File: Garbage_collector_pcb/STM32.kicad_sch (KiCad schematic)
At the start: 26 parts, among them J2 Conn_ST_STDC14, SW2 SW_Push, U2 BQ25896RTWR, Y2 24MHz, Y3 32KHz

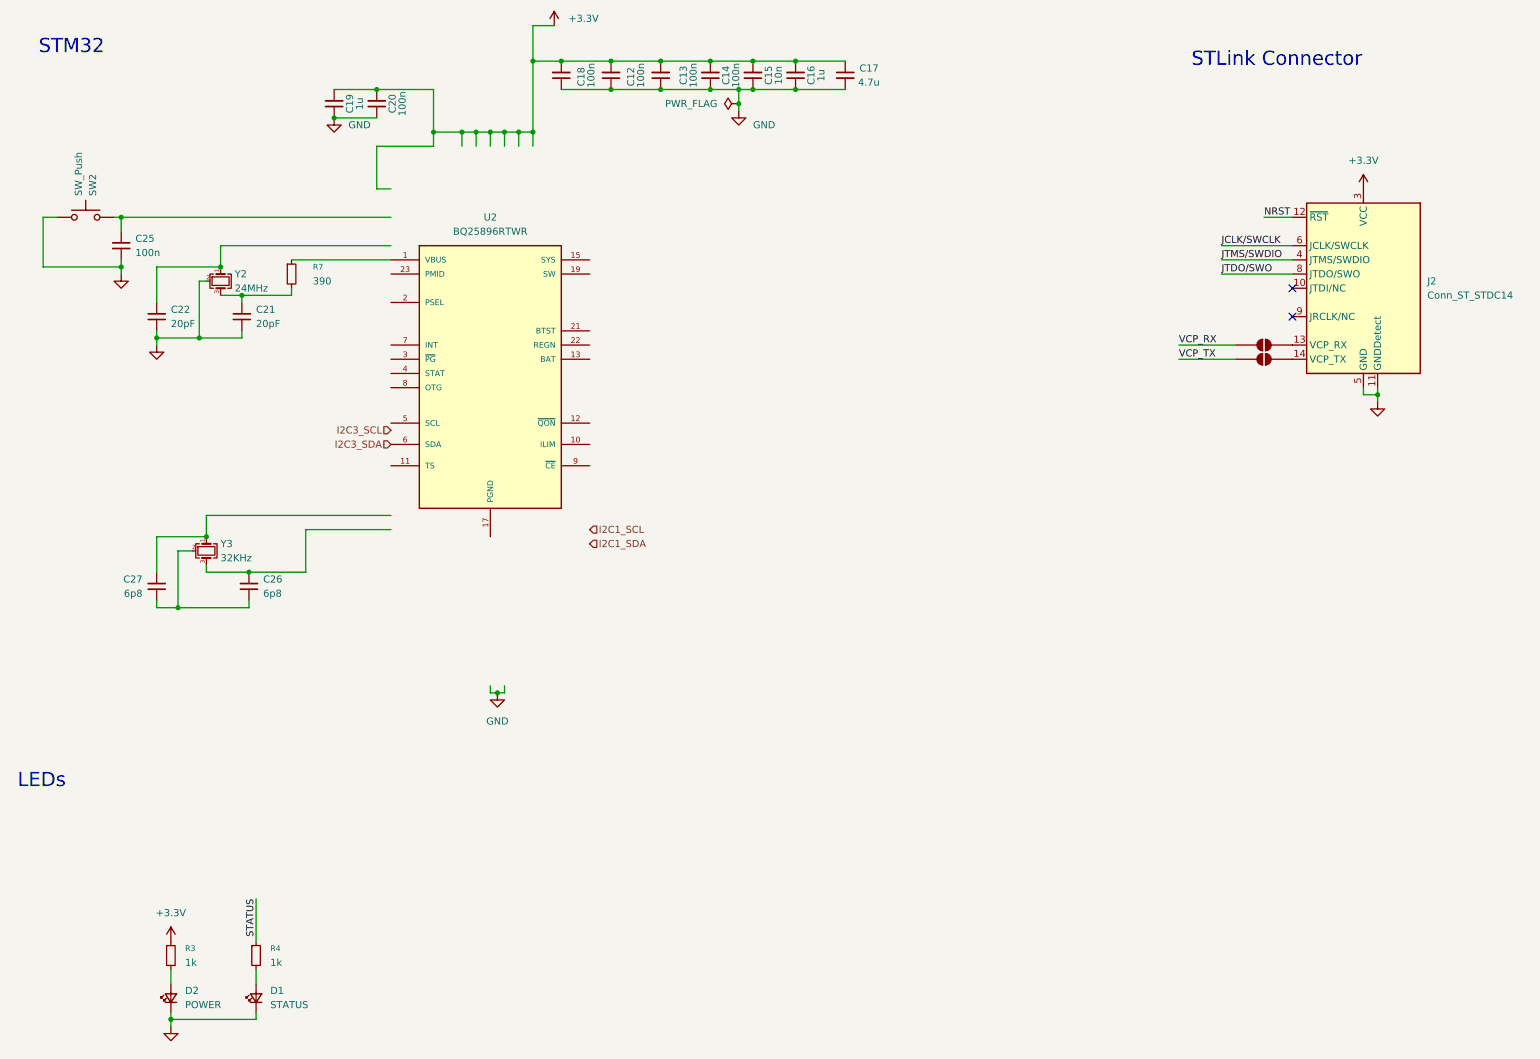
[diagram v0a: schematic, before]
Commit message: update MCU+Moteurs+Capteurs parts + assignement des labels + assignement des pins sur l'ioc (CubeMX)
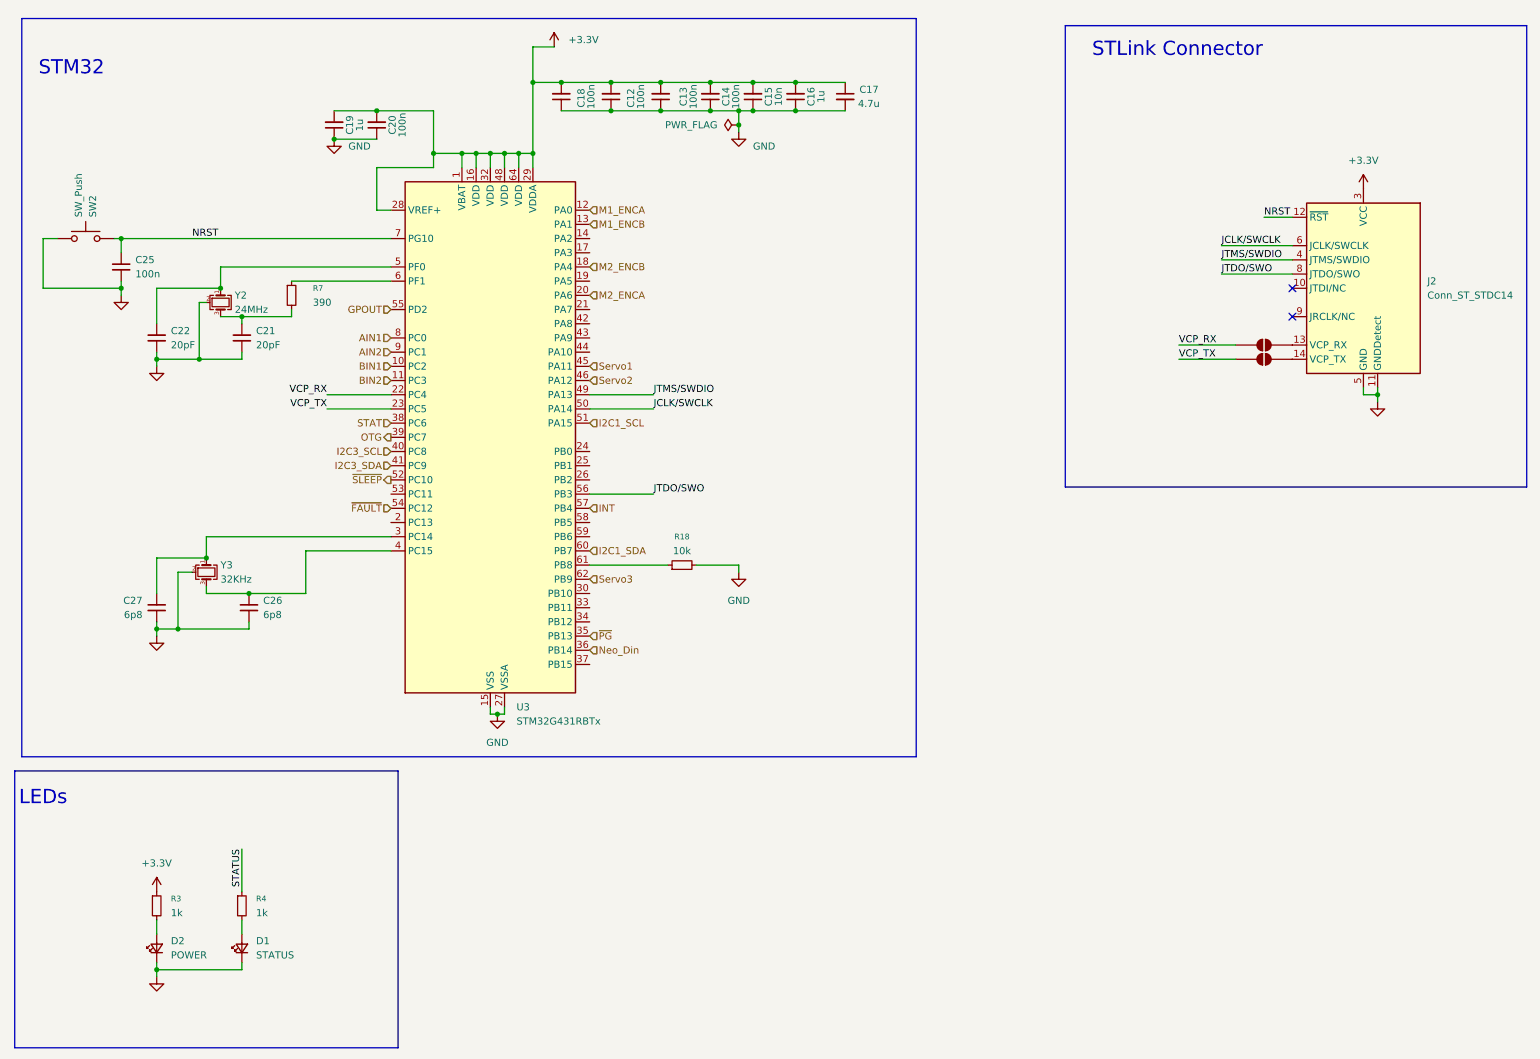
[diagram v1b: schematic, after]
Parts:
- removed U2: BQ25896RTWR, Package_DFN_QFN:Texas_RTW_WQFN-24-1EP_4x4mm_P0.5mm_EP2.7x2.7mm, symbol MCU_ST_STM32G4:STM32G431RBTx
- added R18: 10k, Resistor_THT:R_Array_SIP4, symbol Device:R_Small
- added U3: STM32G431RBTx, Package_QFP:LQFP-64_10x10mm_P0.5mm, symbol MCU_ST_STM32G4:STM32G431RBTx
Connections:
- net +3.3V: now also U3.1 (VBAT), U3.16 (VDD), U3.28 (VREF+), U3.29 (VDDA), U3.32 (VDD), U3.48 (VDD), U3.64 (VDD)
- net GND: now also C26.2, C27.2, Y3.2 (G), Y3.4 (G), R18.2, U3.15 (VSS), U3.27 (VSSA), U3.31 (VSS), U3.47 (VSS), U3.63 (VSS)
- net I2C1_SCL: now also U3.51 (PA15)
- net I2C1_SDA: now also U3.60 (PB7)
- net I2C3_SCL: now also U3.40 (PC8)
- net I2C3_SDA: now also U3.41 (PC9)
- net JCLK/SWCLK: now also U3.50 (PA14)
- net JTDO/SWO: now also U3.56 (PB3)
- net JTMS/SWDIO: now also U3.49 (PA13)
- net NRST: now also C25.1, SW2.1, U3.7 (PG10)
- net VCP_RX: now also U3.22 (PC4)
- net VCP_TX: now also U3.23 (PC5)
- net at C27.1, Y3.1: now also U3.3 (PC14)
- net at C22.1, Y2.1: now also U3.5 (PF0)
- net at R7.1: now also U3.6 (PF1)
- net at C26.1, Y3.3: now also U3.4 (PC15)
- new net: R18.1, U3.61 (PB8)
- new net AIN1: U3.8 (PC0)
- new net AIN2: U3.9 (PC1)
- new net BIN1: U3.10 (PC2)
- new net BIN2: U3.11 (PC3)
- new net GPOUT: U3.55 (PD2)
- new net INT: U3.57 (PB4)
- new net M1_ENCA: U3.12 (PA0)
- new net M1_ENCB: U3.13 (PA1)
- new net M2_ENCA: U3.20 (PA6)
- new net M2_ENCB: U3.18 (PA4)
- new net Neo_Din: U3.36 (PB14)
- new net OTG: U3.39 (PC7)
- new net STAT: U3.38 (PC6)
- new net Servo1: U3.45 (PA11)
- new net Servo2: U3.46 (PA12)
- new net Servo3: U3.62 (PB9)
- new net ~{FAULT}: U3.54 (PC12)
- new net ~{PG}: U3.35 (PB13)
- new net ~{SLEEP}: U3.52 (PC10)
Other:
- moved on the sheet: C12, C13, C14, C15, C16, C17, C18, C19, C20, C21, C22, C25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

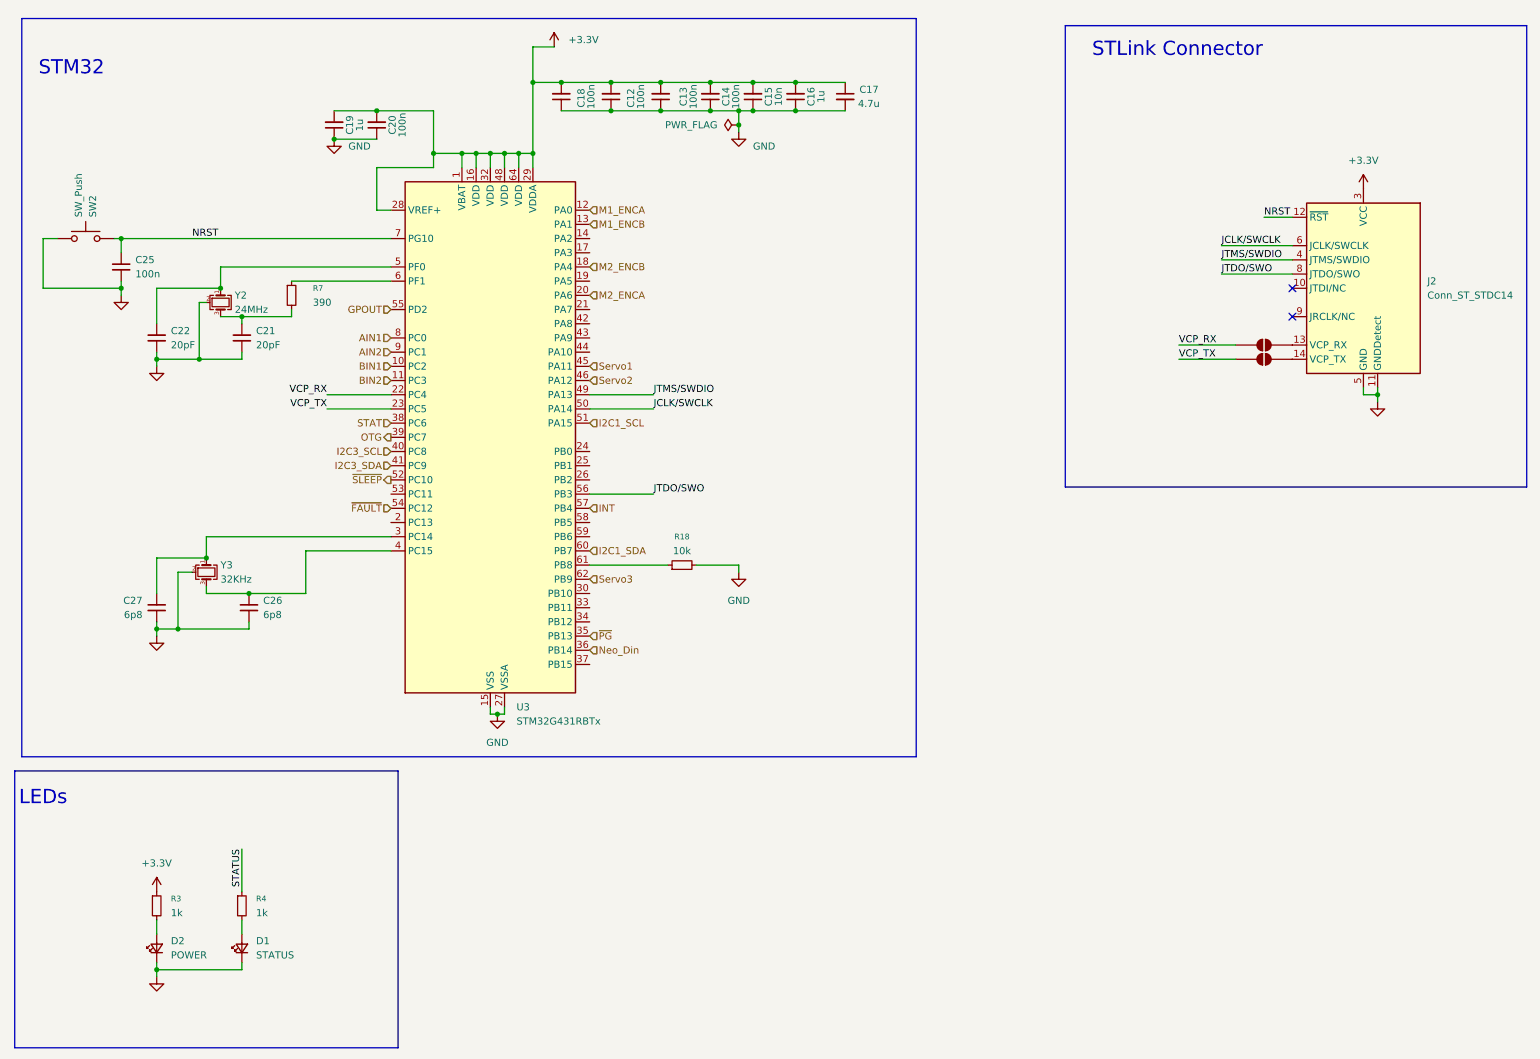
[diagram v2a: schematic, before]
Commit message: update schematic
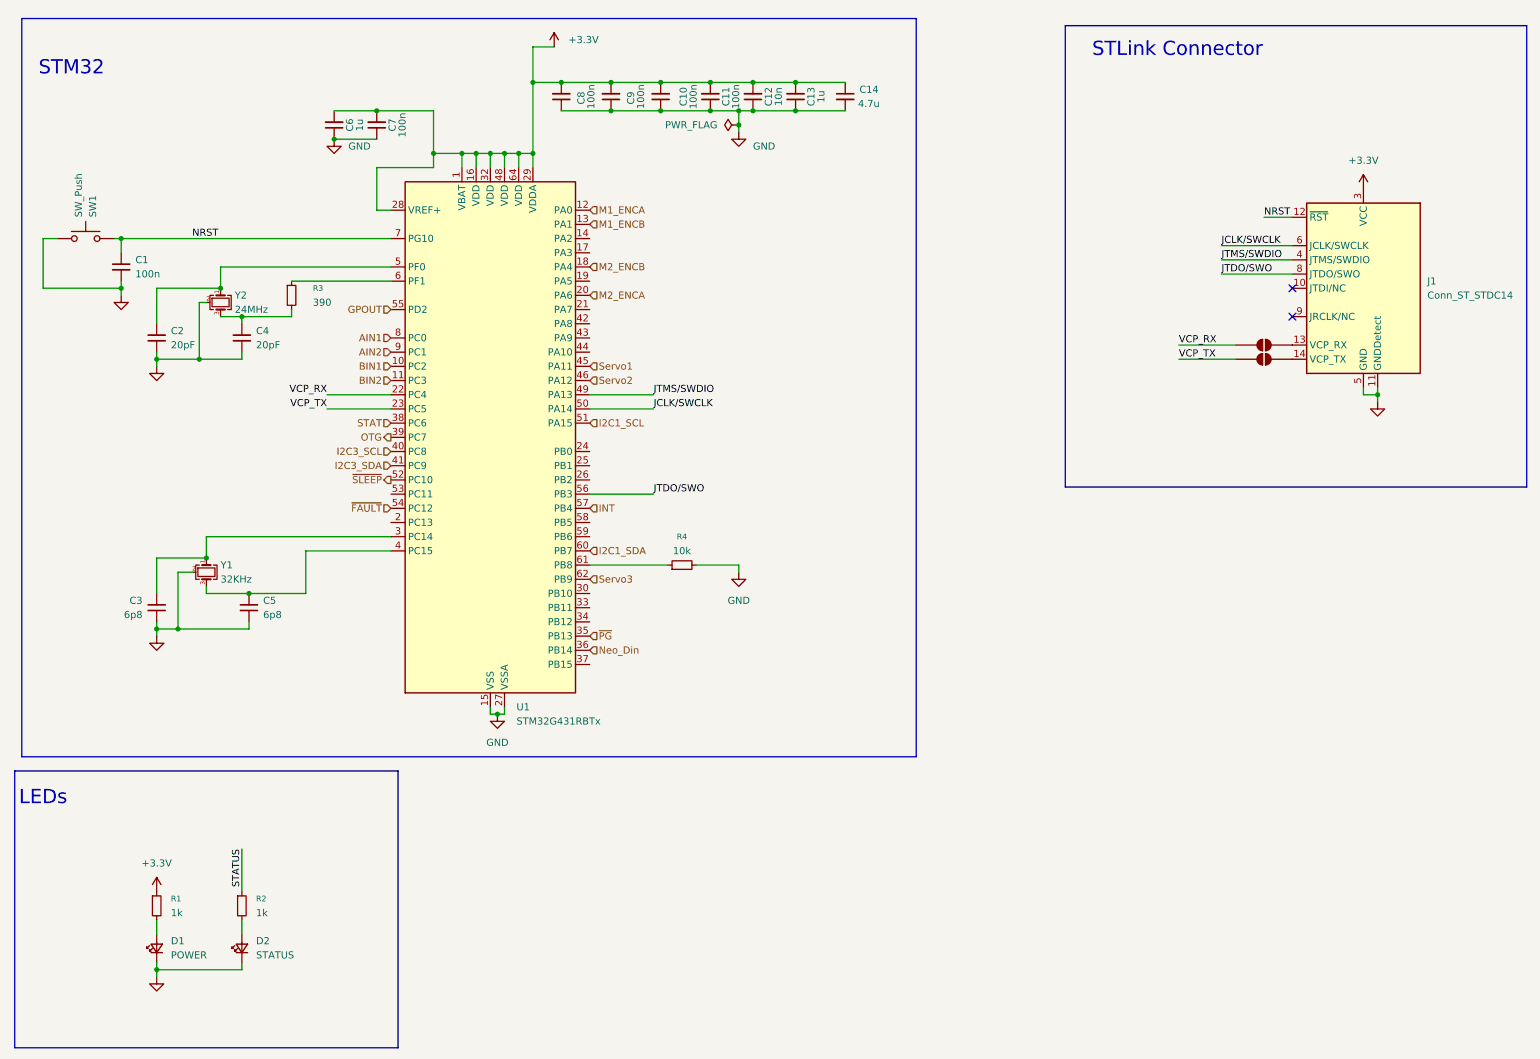
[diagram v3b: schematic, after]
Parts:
- renumbered C25 to C1, C13 to C10, C14 to C11, C15 to C12, C16 to C13, C17 to C14, C22 to C2, C27 to C3, C21 to C4, C26 to C5, C19 to C6, C20 to C7, C18 to C8, C12 to C9, D2 to D1, D1 to D2, J2 to J1, R3 to R1, R4 to R2, R7 to R3, R18 to R4, SW2 to SW1, U3 to U1, Y3 to Y1

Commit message: ajout du ioc et schema validé
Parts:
- removed C3, C5: 6p8, Capacitor_SMD:C_0402_1005Metric, symbol Device:C_Small
- removed D1: POWER, LED_SMD:LED_0603_1608Metric, symbol Device:LED_Small
- removed D2: STATUS, LED_SMD:LED_0603_1608Metric, symbol Device:LED_Small
- removed JP1, JP2: SolderJumper_2_Open, Jumper:SolderJumper-2_P1.3mm_Open_TrianglePad1.0x1.5mm, symbol Jumper:SolderJumper_2_Open
- removed R1, R2: 1k, Resistor_SMD:R_0402_1005Metric, symbol Device:R_Small
- removed R4: 10k, Resistor_THT:R_Array_SIP4, symbol Device:R_Small
- removed Y1: 32KHz, Crystal:Crystal_SMD_EuroQuartz_MT-4Pin_3.2x2.5mm, symbol Device:Crystal_GND24_Small
- added J10: NRF52840, Connector_JST:JST_GH_BM03B-GHS-TBT_1x03-1MP_P1.25mm_Vertical, symbol Kicad:Conn_01x04
- C10, C11, C7, C8, C9: footprint Capacitor_SMD:C_0402_1005Metric_Pad0.74x0.62mm_HandSolder -> Capacitor_SMD:C_0402_1005Metric; JLCPCB Part # (none) -> C1525
- C12: value 10n -> 4u7; footprint Capacitor_SMD:C_0402_1005Metric_Pad0.74x0.62mm_HandSolder -> Capacitor_SMD:C_0402_1005Metric; JLCPCB Part # (none) -> C23733
- C13: value 1u -> 10n; footprint Capacitor_SMD:C_0402_1005Metric_Pad0.74x0.62mm_HandSolder -> Capacitor_SMD:C_0402_1005Metric; JLCPCB Part # (none) -> C15195
- C14: value 4.7u -> 1u; footprint Capacitor_SMD:C_0402_1005Metric_Pad0.74x0.62mm_HandSolder -> Capacitor_SMD:C_0402_1005Metric; JLCPCB Part # (none) -> C52923
- C6: footprint Capacitor_SMD:C_0402_1005Metric_Pad0.74x0.62mm_HandSolder -> Capacitor_SMD:C_0402_1005Metric; JLCPCB Part # (none) -> C14445
- R3: JLCPCB Part # (none) -> C22356179
- SW1: JLCPCB Part # (none) -> C72443
- U1: JLCPCB Part # (none) -> C431633
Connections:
- net +3.3V: now also C10.1, C11.1, C12.1, C13.1, C8.1, C9.1, J10.1 (Pin_1); no longer C10.2, C11.2, C12.2, C13.2, C8.2, C9.2
- net GND: now also C10.2, C11.2, C12.2, C13.2, C8.2, C9.2, J10.4 (Pin_4); no longer C10.1, C11.1, C12.1, C13.1, C8.1, C9.1
- net I2C1_SCL: now also U1.61 (PB8); no longer U1.51 (PA15)
- net VCP_RX: now also J1.13 (VCP_RX), U1.17 (PA3); no longer U1.22 (PC4)
- net VCP_TX: now also J1.14 (VCP_TX), U1.14 (PA2); no longer U1.23 (PC5)
- net MOTOR_SLEEP: now reaches U1.2 (PC13)
- net TOF1_INT: now reaches U1.30 (PB10)
- net TOF1_XST: now reaches U1.33 (PB11)
- net TOF2_INT: now reaches U1.34 (PB12)
- net USART3_RX: now reaches U1.53 (PC11)
- net USART3_RX: now also J10.3 (Pin_3)
- net CHARGEUR_PG: now reaches U1.58 (PB5)
- net CHARGEUR_QON: now reaches U1.59 (PB6)
- net GPOUT renamed FG_GPIO
- net INT renamed CHARGEUR_INT
- net OTG: no longer names the net of U1.39 (PC7)
- net STAT renamed Lidar_M_CTRL
- net Servo3 renamed COLOR_INT
- net ~{FAULT} renamed MOTOR_FAULT
- net ~{PG} renamed TOF2_XST
- net ~{SLEEP} renamed USART3_TX
- net USART3_TX: now also J10.2 (Pin_2)
- new net Lidar_TX: U1.23 (PC5)
- no-connect marks 2 -> 16
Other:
- note added: "Comm sans fil"
- note removed: "LEDs"
- moved on the sheet: C6, C7
